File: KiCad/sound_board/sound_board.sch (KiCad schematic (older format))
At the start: 15 parts, among them P101 CONN_01X06, P102 CONN_01X06, P103 CONN_01X06, U101 MCP45HVx1, U102 MCP45HVx1, U103 DS1808

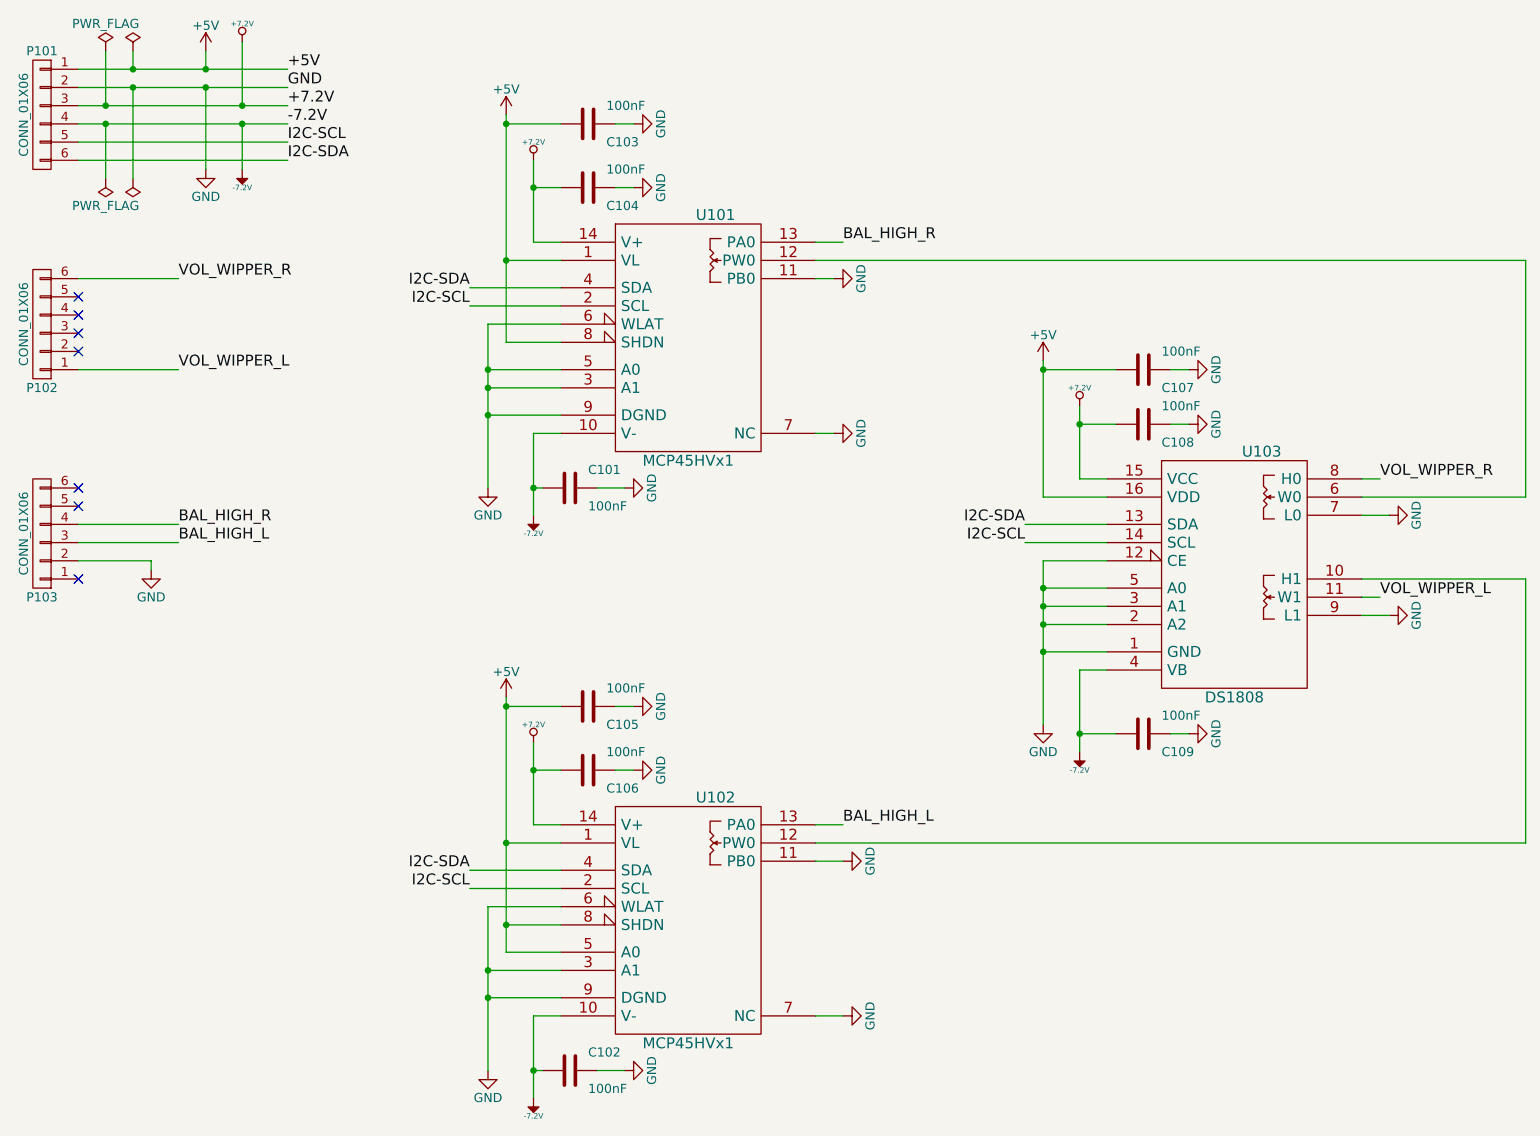
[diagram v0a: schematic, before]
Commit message: Only one i2c potentiometer to manage sound
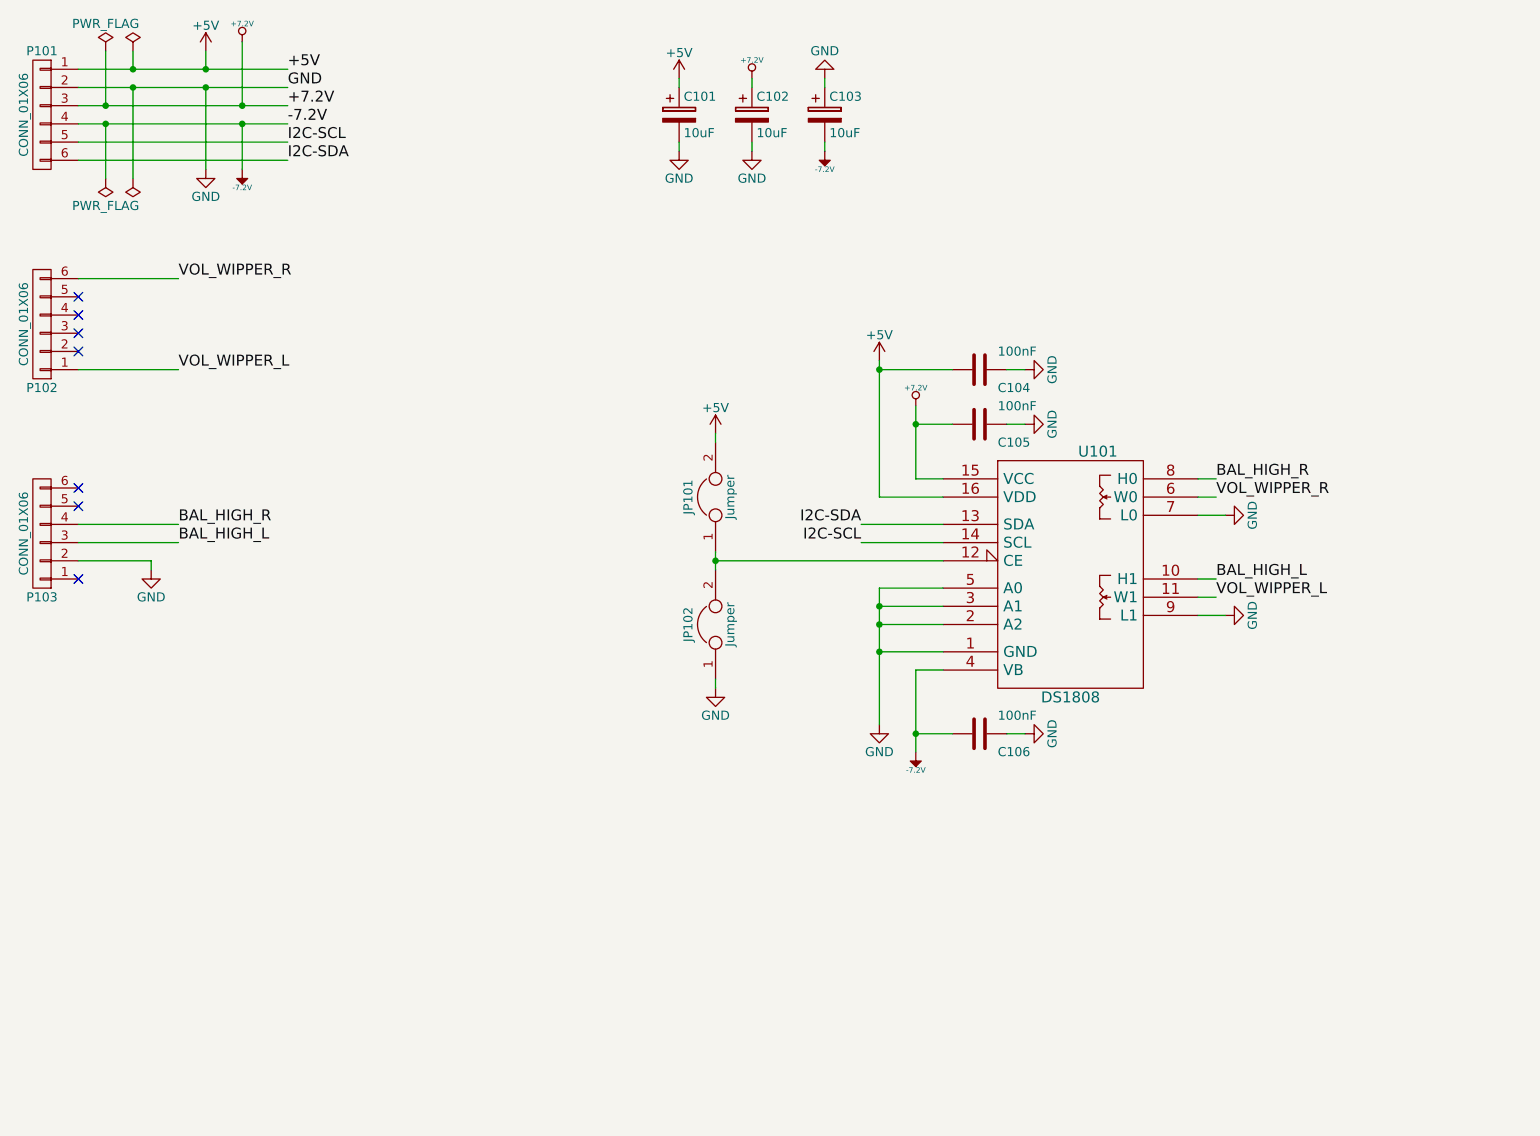
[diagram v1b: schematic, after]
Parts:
- removed C101, C102, C103, C104, C105, C106: 100nF, Capacitors_SMD:C_0603_HandSoldering, symbol C
- removed U101, U102: MCP45HVx1, Housings_SSOP:TSSOP-14_4.4x5mm_Pitch0.65mm, symbol MCP45HVx1
- added C101, C102, C103: 10uF, Capacitors_ThroughHole:CP_Radial_D5.0mm_P2.50mm, symbol CP
- added JP101, JP102: Jumper, Measurement_Points:Test_Point_2Pads, symbol Jumper
- renumbered C107 to C104, C108 to C105, C109 to C106, U103 to U101
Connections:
- net +5V: now also C101.1, JP101.2
- net +7.2V: now also C102.1
- net -7.2V: now also C103.2
- net BAL_HIGH_L: now also U101.10 (H1)
- net BAL_HIGH_R: now also U101.8 (H0)
- net GND: now also C101.2, C102.2, C103.1, JP102.1; no longer U101.12 (CE)
- net VOL_WIPPER_R: now also U101.6 (W0); no longer U101.8 (H0)
- new net: JP101.1, JP102.2, U101.12 (CE)
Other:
- moved on the sheet: C104, C105, C106, U101
